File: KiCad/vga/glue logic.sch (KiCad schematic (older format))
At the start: 6 parts, among them U10 74HC245, U11 74HC245, U6 74HC245, U7 74HC245, U8 74HC245, U9 74HC245

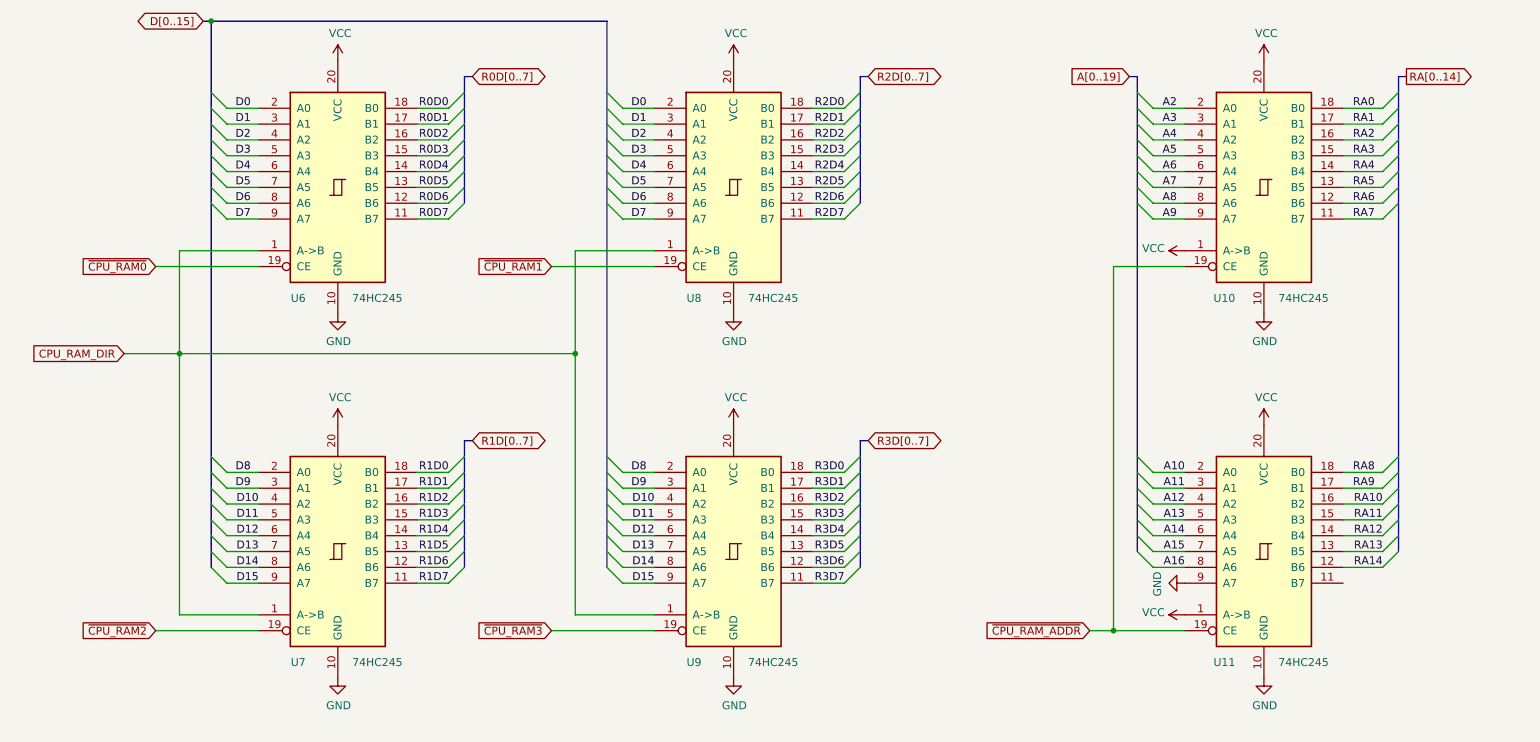
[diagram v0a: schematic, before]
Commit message: Updated graphics adapter and main schematics + board.
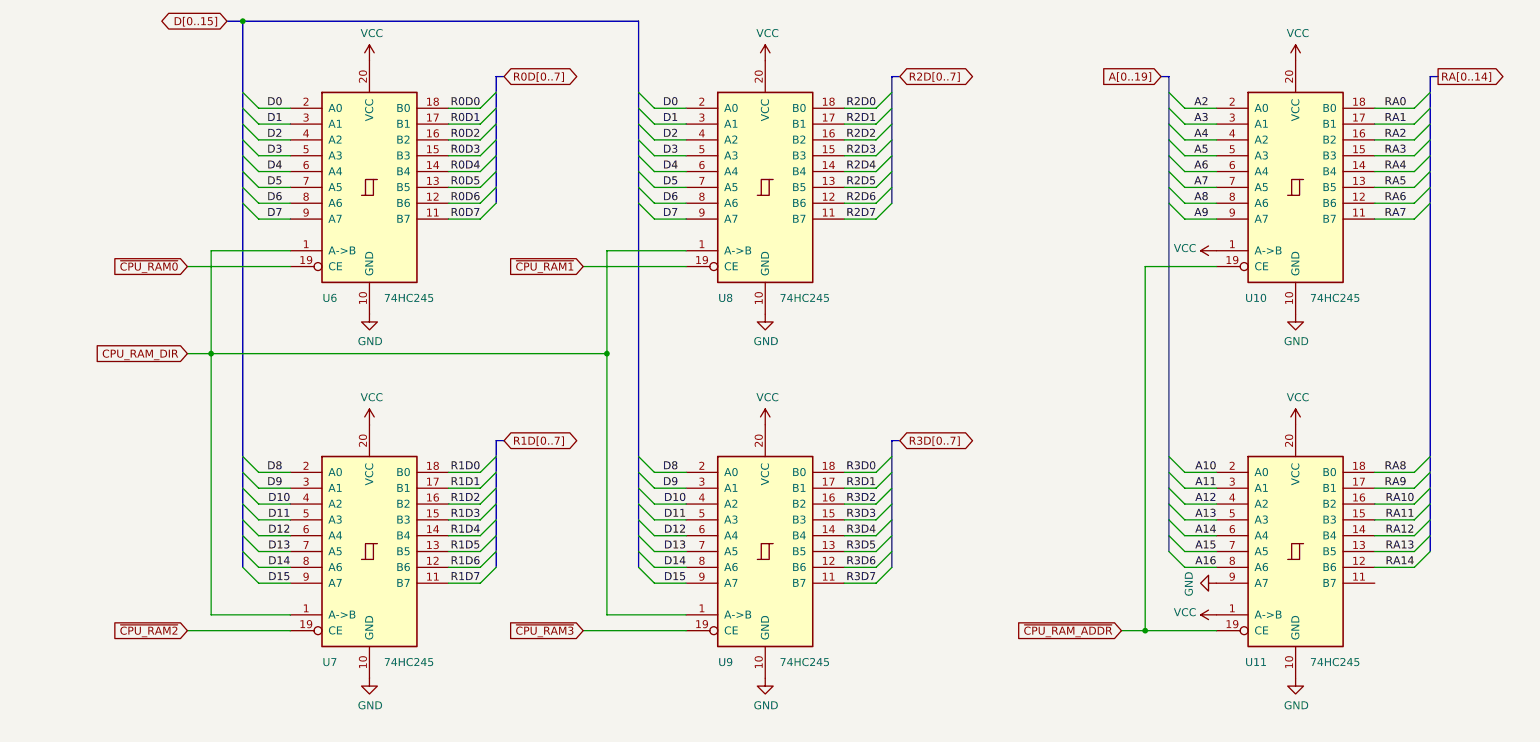
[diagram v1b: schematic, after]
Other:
- moved on the sheet: U10, U11, U6, U7, U8, U9

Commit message: Updated KiCad VGA board and main board.
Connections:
- no-connect marks 0 -> 1
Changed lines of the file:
@@
 Text GLabel 4350 5150 0    50   Input ~ 0
 ~CPU_RAM3
+NoConn ~ 9350 4850
 Wire Bus Line
 	6300 3950 6300 4750

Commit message: Updated graphics adapter
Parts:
- added R12: 4K7, Resistor_THT:R_Axial_DIN0204_L3.6mm_D1.6mm_P7.62mm_Horizontal, symbol Device:R
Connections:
- net GND: now also R12.2; no longer U11.9 (A7)
- new net: R12.1, U11.9 (A7)
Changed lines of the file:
@@
 A16
-$Comp
-L power:GND #PWR040
-U 1 1 5F8495EC
-P 8350 4850
-F 0 "#PWR040" H 8350 4600 50  0001 C CNN
-F 1 "GND" H 8355 4677 50  0000 C CNN
-F 2 "" H 8350 4850 50  0001 C CNN
-F 3 "" H 8350 4850 50  0001 C CNN
-	1    8350 4850
-	0    1    1    0
-$EndComp
 $Comp
 L power:VCC #PWR041
@@
 ~CPU_RAM3
 NoConn ~ 9350 4850
+Wire Wire Line
+	8000 4850 8350 4850
 Wire Bus Line
 	6300 3950 6300 4750
@@
 Wire Bus Line
 	2200 1300 2200 4750
+$Comp
+L power:GND #PWR040
+U 1 1 5F98D1E5
+P 8000 5550
+F 0 "#PWR040" H 8000 5300 50  0001 C CNN
+F 1 "GND" H 8005 5377 50  0000 C CNN
+F 2 "" H 8000 5550 50  0001 C CNN
+F 3 "" H 8000 5550 50  0001 C CNN
+	1    8000 5550
+	1    0    0    -1
+$EndComp
+Wire Wire Line
+	8000 5250 8000 4850
+$Comp
+L Device:R R12
+U 1 1 5F978CEC
+P 8000 5400
+F 0 "R12" H 8070 5446 50  0000 L CNN
+F 1 "4K7" H 8070 5355 50  0000 L CNN
+F 2 "Resistor_THT:R_Axial_DIN0204_L3.6mm_D1.6mm_P7.62mm_Horizontal" V 7930 5400 50  0001 C CNN
+F 3 "~" H 8000 5400 50  0001 C CNN
+	1    8000 5400
+	1    0    0    -1
+$EndComp
 $EndSCHEMATC

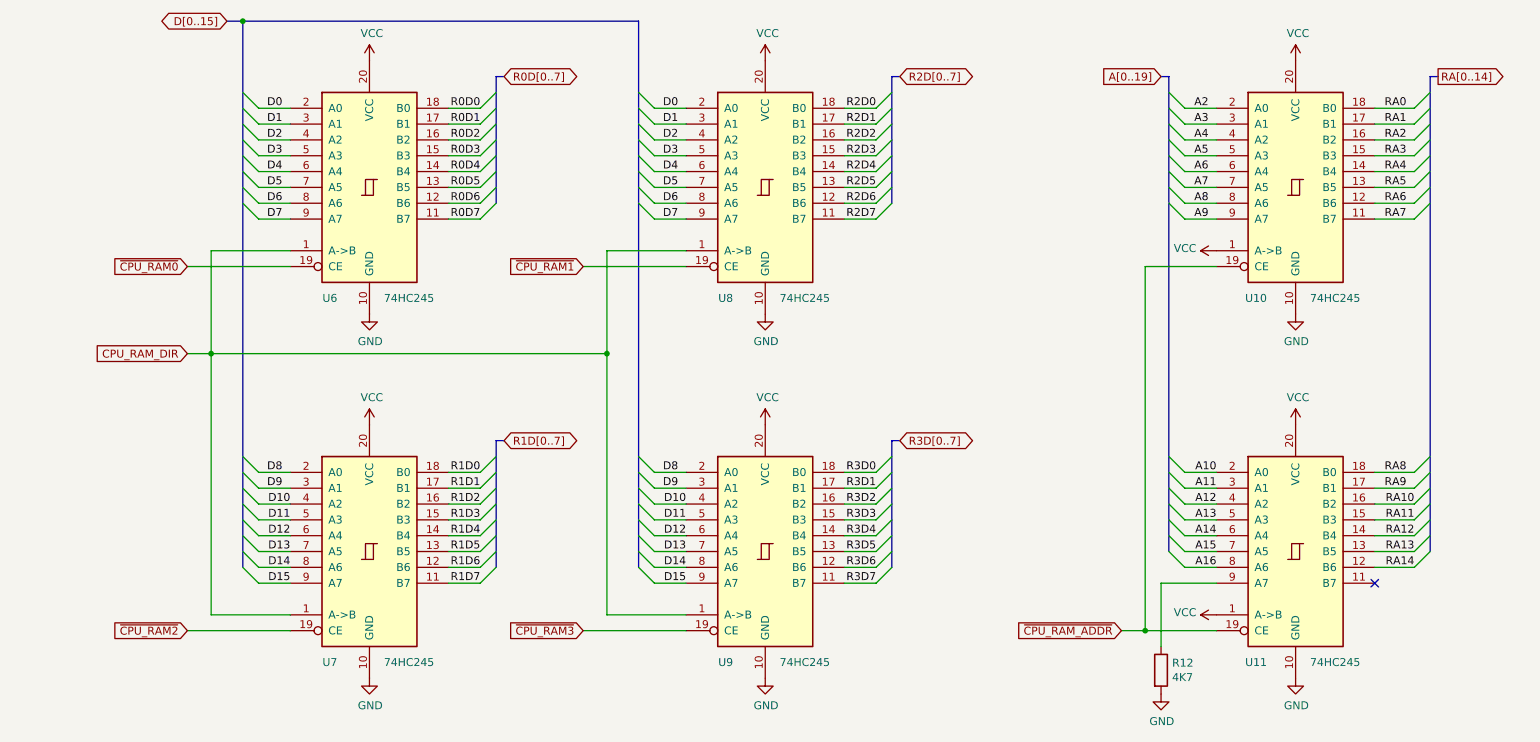
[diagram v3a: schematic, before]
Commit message: Replaced MAX7000 CPLD with MAX II in graphics adapter. PCB redesign with smaller size.
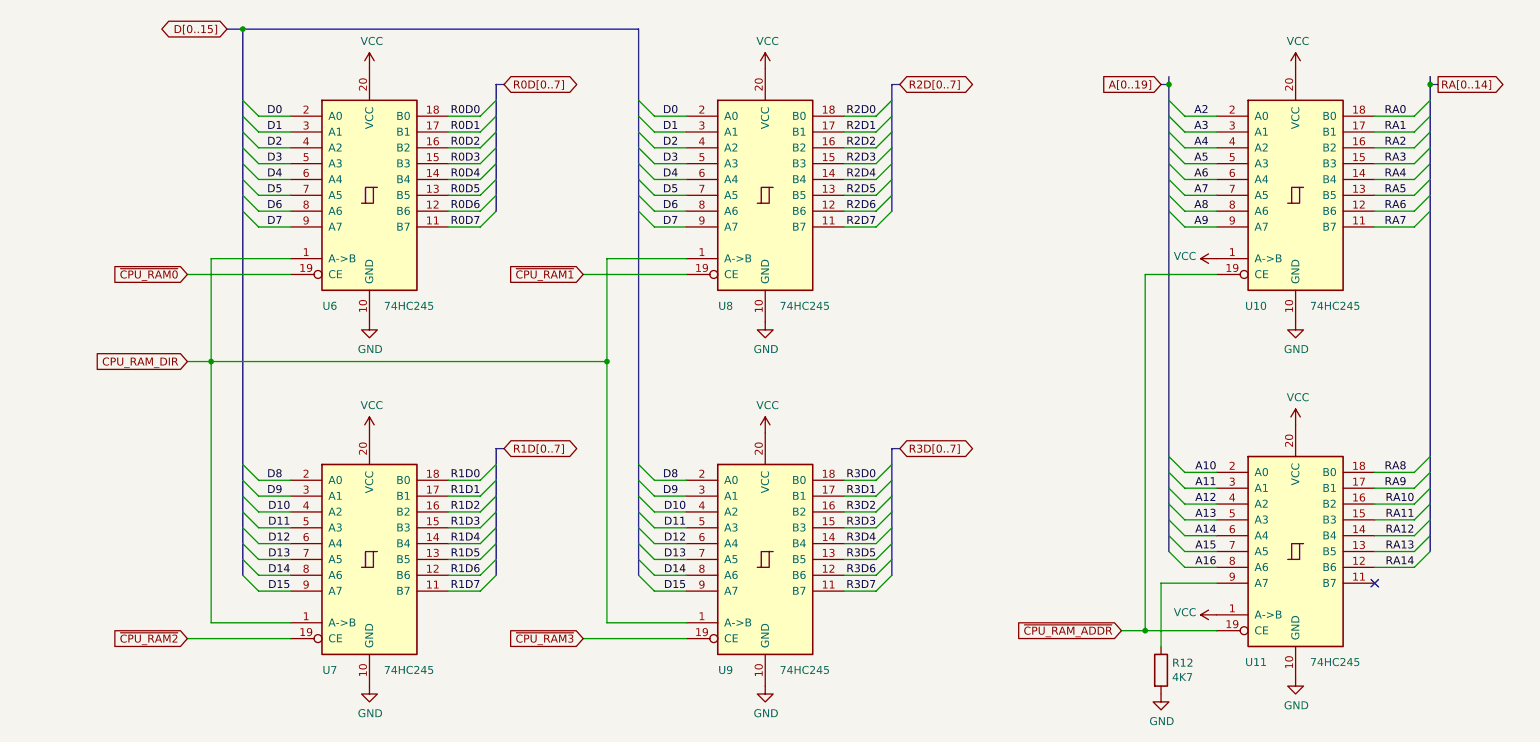
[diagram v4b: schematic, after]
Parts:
- R12: footprint Resistor_THT:R_Axial_DIN0204_L3.6mm_D1.6mm_P7.62mm_Horizontal -> Resistor_THT:R_Axial_DIN0207_L6.3mm_D2.5mm_P2.54mm_Vertical
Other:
- moved on the sheet: U10, U6, U7, U8, U9

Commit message: Finished VGA adapter Rev. 1.0
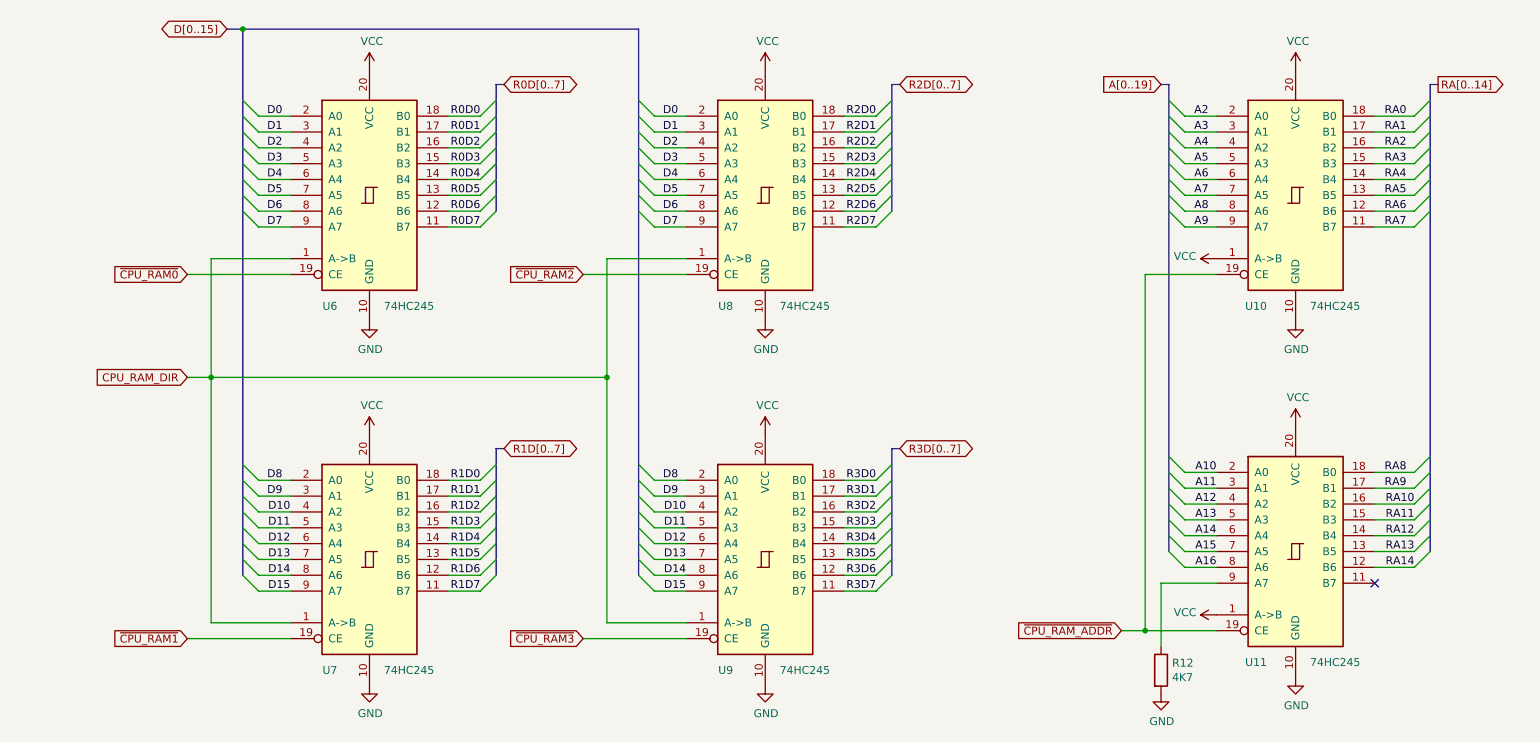
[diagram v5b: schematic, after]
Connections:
- net ~CPU_RAM1: now also U7.19 (CE); no longer U8.19 (CE)
- net ~CPU_RAM2: now also U8.19 (CE); no longer U7.19 (CE)
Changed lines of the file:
@@
 R3D7
 Wire Wire Line
-	4500 3450 4500 2800
+	4500 3550 4500 2800
 Wire Wire Line
 	4500 2800 5000 2800
 Wire Wire Line
-	4500 3450 4500 5100
+	4500 3550 4500 5100
 Wire Wire Line
 	4500 5100 5000 5100
-Connection ~ 4500 3450
+Connection ~ 4500 3550
 Wire Wire Line
 	2500 5100 2000 5100
 Wire Wire Line
-	2000 5100 2000 3450
+	2000 5100 2000 3550
 Wire Wire Line
 	2000 2800 2500 2800
 Wire Wire Line
-	2000 3450 4500 3450
-Connection ~ 2000 3450
-Wire Wire Line
-	2000 3450 2000 2800
-Wire Wire Line
-	2000 3450 1850 3450
-Text GLabel 1850 3450 0    50   Input ~ 0
+	2000 3550 4500 3550
+Connection ~ 2000 3550
+Wire Wire Line
+	2000 3550 2000 2800
+Wire Wire Line
+	2000 3550 1850 3550
+Text GLabel 1850 3550 0    50   Input ~ 0
 CPU_RAM_DIR
 Wire Wire Line
@@
 ~CPU_RAM0
 Text GLabel 4350 2900 0    50   Input ~ 0
+~CPU_RAM2
+Text GLabel 1850 5200 0    50   Input ~ 0
 ~CPU_RAM1
-Text GLabel 1850 5200 0    50   Input ~ 0
-~CPU_RAM2
 Text GLabel 4350 5200 0    50   Input ~ 0
 ~CPU_RAM3
-Wire Bus Line
-	8050 1650 8050 1700
-Wire Bus Line
-	9700 1650 9700 1700
 $Comp
 L Device:R R12
@@
 	1    0    0    -1
 $EndComp
-Connection ~ 8050 1700
-Connection ~ 9700 1700
 Wire Bus Line
 	6300 4000 6300 4800
